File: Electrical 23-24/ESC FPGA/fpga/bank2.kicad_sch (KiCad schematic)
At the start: 54 parts, among them SW1 SW_SPDT, SW2 SW_Push, U14 FXMA108BQX, U16 XC6SLX9-TQG144, X1 KC5032Z100.000C1JX00

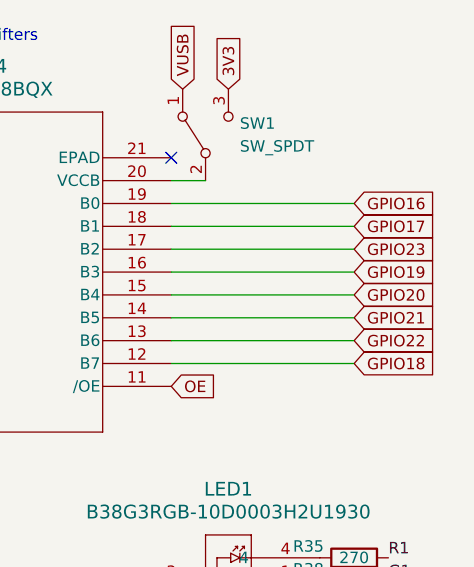
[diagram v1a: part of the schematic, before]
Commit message: Finished hard signal routing, need PMOD and Power
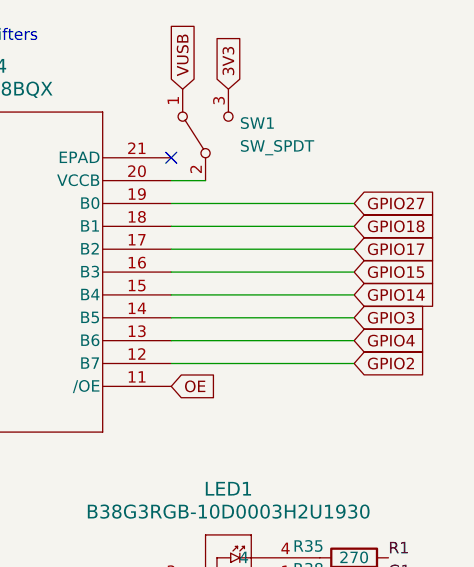
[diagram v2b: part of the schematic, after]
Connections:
- net GPIO23 is gone; now on net GPIO17: U14.17 (B2)
- net GPIO17: no longer U14.18 (B1)
- net GPIO18: now also U14.18 (B1); no longer U14.12 (B7)
- net GPIO16 renamed GPIO27
- net GPIO19 renamed GPIO15
- net GPIO20 renamed GPIO14
- net GPIO21 renamed GPIO3
- net GPIO22 renamed GPIO4
- new net GPIO2: U14.12 (B7)

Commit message: Finish PCB layout, need to DRC
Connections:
- net PMOD1_1: now also U16.17 (IO_L43P_GCLK23_3); no longer U16.21 (IO_L42N_GCLK24_3)
- net PMOD1_2: now also U16.15 (IO_L44P_GCLK21_3); no longer U16.17 (IO_L43P_GCLK23_3)
- net PMOD1_4: now also U16.21 (IO_L42N_GCLK24_3); no longer U16.16 (IO_L43N_GCLK22_IRDY2_3)
- net PMOD1_5: now also U16.16 (IO_L43N_GCLK22_IRDY2_3); no longer U16.15 (IO_L44P_GCLK21_3)
- net PMOD2_1: now also U16.8 (IO_L51P_3); no longer U16.9 (IO_L50N_3)
- net PMOD2_2: now also U16.6 (IO_L52P_3); no longer U16.8 (IO_L51P_3)
- net PMOD2_3: now also U16.2 (IO_L83P_3); no longer U16.7 (IO_L51N_3)
- net PMOD2_4: now also U16.9 (IO_L50N_3); no longer U16.6 (IO_L52P_3)
- net PMOD2_5: now also U16.7 (IO_L51N_3); no longer U16.5 (IO_L52N_3)
- net PMOD2_6: now also U16.5 (IO_L52N_3); no longer U16.2 (IO_L83P_3)
- net SW2: now also U16.34 (IO_L1N_VREF_3); no longer U16.35 (IO_L1P_3)
- net SW3: now also U16.35 (IO_L1P_3); no longer U16.34 (IO_L1N_VREF_3)
